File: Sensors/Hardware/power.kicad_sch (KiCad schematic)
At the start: 20 parts, among them U6 LM66200DRLR, U7 MAX77827AEFD+T, U8 SC4215

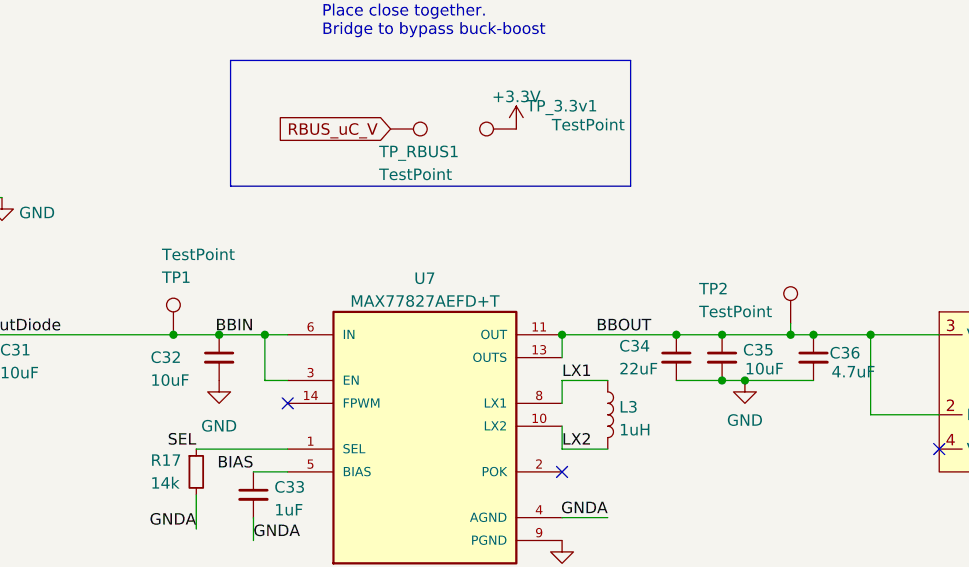
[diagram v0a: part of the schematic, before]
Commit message: Silkscreen for all fps and back plate
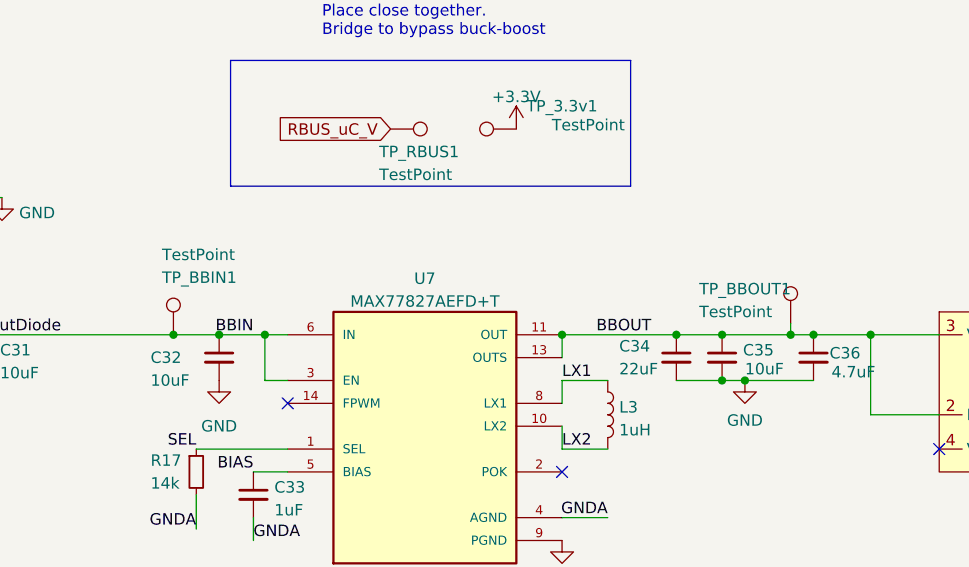
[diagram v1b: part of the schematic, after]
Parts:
- renumbered TP1 to TP_BBIN1, TP2 to TP_BBOUT1
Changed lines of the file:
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@@
   (symbol (lib_id "Connector:TestPoint") (at 137.16 57.15 0) (unit 1)
     (in_bom yes) (on_board yes) (dnp no)
-    (property "Reference" "TP1" (at 135.89 50.8 0)
+    (property "Reference" "TP_BBIN1" (at 135.89 50.8 0)
       (effects (font (size 1.27 1.27)) (justify left))
     )
@@
       (project "sensorboard"
         (path "/26801cfb-b53b-4a6a-a2f4-5f4986565765/2b173291-6fb0-491b-9706-884a6390c6a8"
-          (reference "TP1") (unit 1)
+          (reference "TP_BBIN1") (unit 1)
         )
       )
@@
   (symbol (lib_id "Connector:TestPoint") (at 205.74 55.88 0) (unit 1)
     (in_bom yes) (on_board yes) (dnp no)
-    (property "Reference" "TP2" (at 195.58 52.07 0)
+    (property "Reference" "TP_BBOUT1" (at 195.58 52.07 0)
       (effects (font (size 1.27 1.27)) (justify left))
     )
@@
       (project "sensorboard"
         (path "/26801cfb-b53b-4a6a-a2f4-5f4986565765/2b173291-6fb0-491b-9706-884a6390c6a8"
-          (reference "TP2") (unit 1)
-        )
-      )
+          (reference "TP_BBOUT1") (unit 1)
+        )
+      )
